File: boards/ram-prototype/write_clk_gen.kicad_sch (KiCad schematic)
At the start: 24 parts, among them U1 74LVC1G00, U2 74LVC1G00, U3 74LVC1G00, U4 74LVC1G00, U5 74LVC1G00, U6 74LVC1G00, U7 74LVC1G00, U8 74LVC1G00

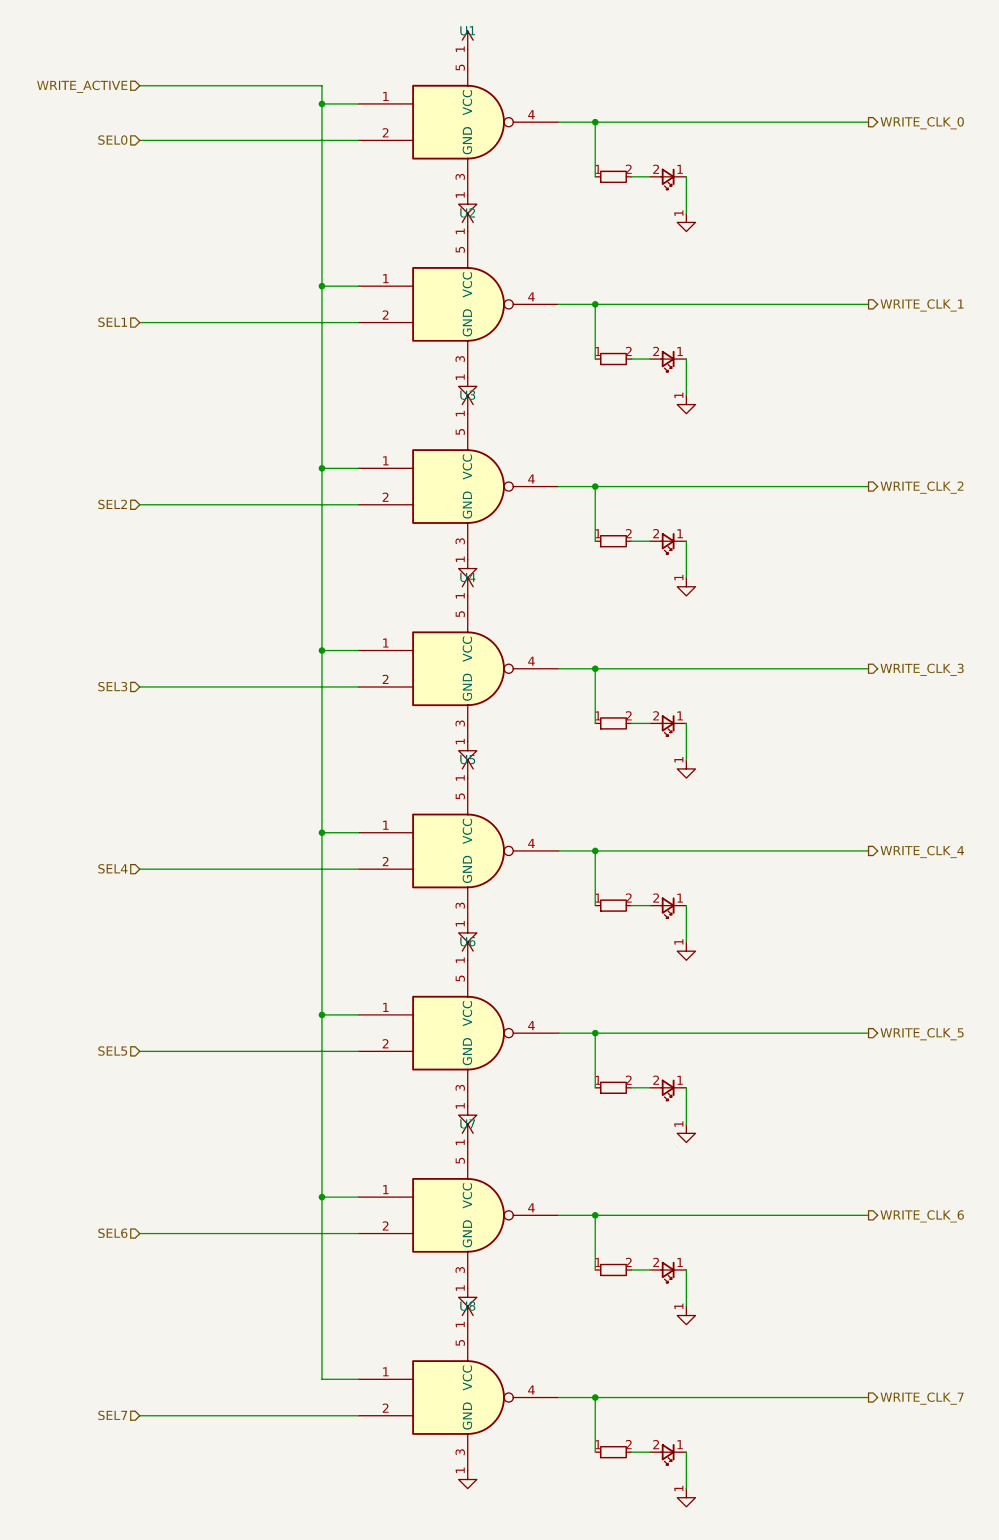
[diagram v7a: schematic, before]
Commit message: Fix labelling
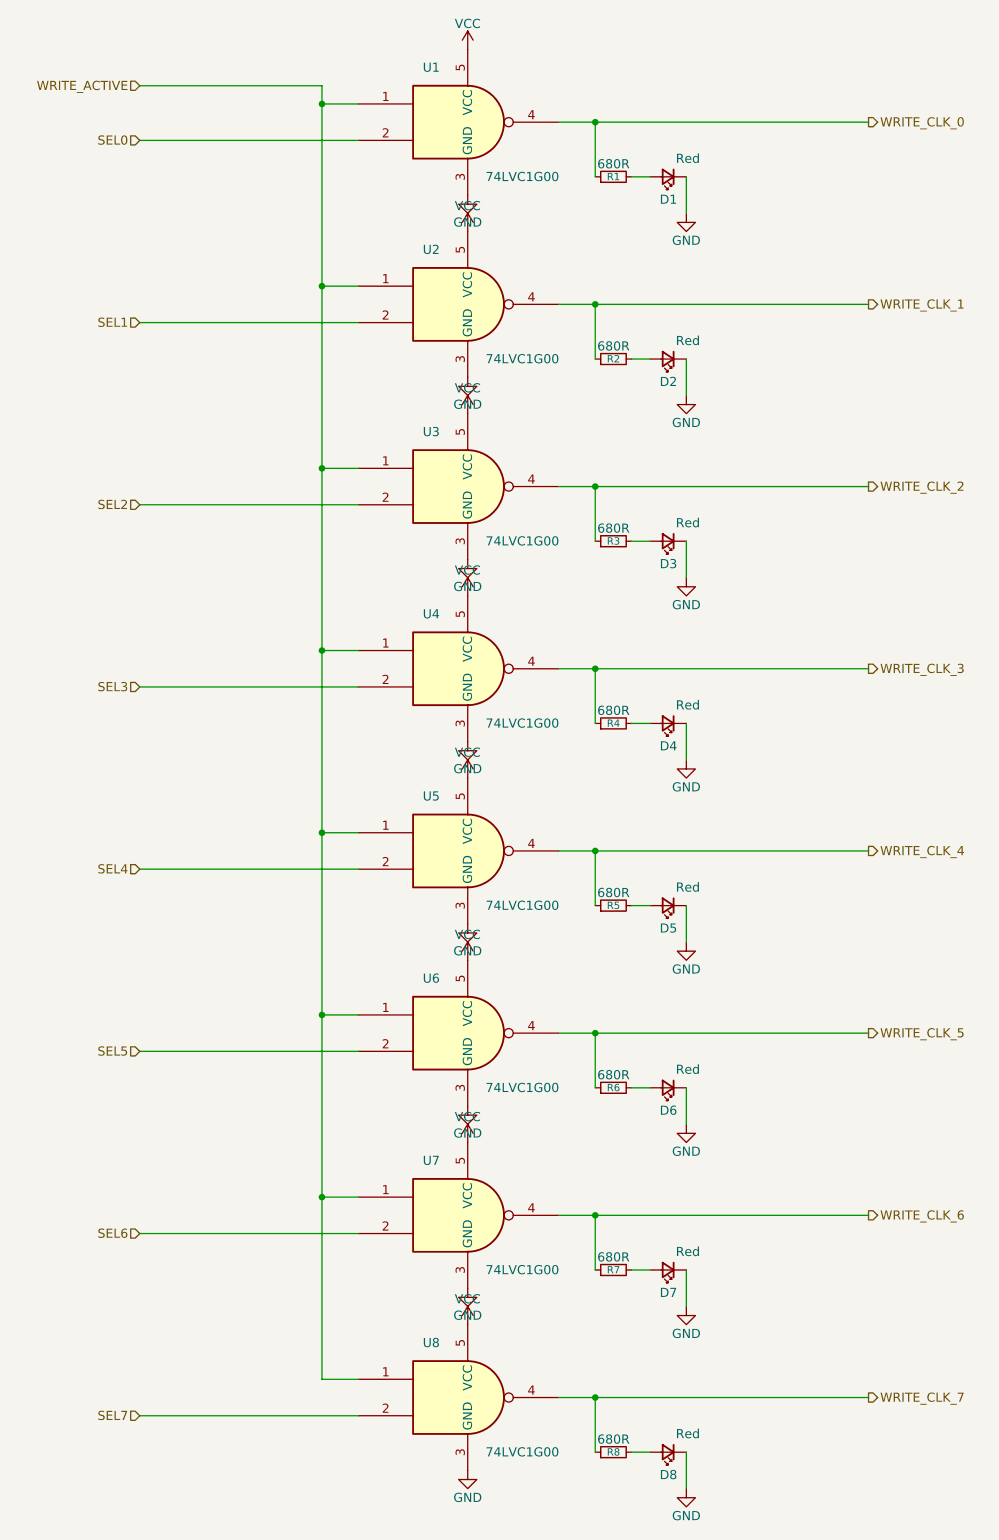
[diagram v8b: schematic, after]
